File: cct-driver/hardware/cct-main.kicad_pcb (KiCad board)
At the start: 2 copper layers, 130 x 164 mm, 217 parts, among them J1 C707824, J10 C37815, J11 C474923, J2 C165948, J3 C441333, J4 C441333, J5 C441333, J6 C441333, J7 C441333, J8 C441333, J9 C2906270, Q1 C3281500, Q10 C2890395, Q11 C2890395, Q12 C2890395, Q13 C2890395, Q14 C2890395, Q15 C2890395, Q16 C2890395, Q17 C2890395, Q18 C2890395, Q2 C3281500, Q3 C20526, Q4 C2146, Q5 C2146, Q6 C20526, Q7 C2890395, Q8 C2890395, Q9 C2890395, SW1 C318884, SW2 C318884, U1 C2864837, U2 C524806, U3 C6186, U4 C701341, U5 C84681, U6 C52140501, U7 C52140501

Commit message: v2 布线:逻辑区的近距离连线铺了一批,未连接 133 → 114,短路仍然是 0
新增一个 `wire()` 小工具:按顺序把同一个网络的几只脚串起来,支持 L 形与 Z 形拐角。
用它铺完了「两脚就在隔壁」的那批线:干接点四路(端子 → 串阻 → 上拉 + 消抖)、
I2C 上拉、Type-C 的 CC 下拉、状态灯、buck 的 FB 分压。

**踩到并记下来的一条**:这些两端元件的**另一只脚常常正好落在 L 形的拐角上** ——
所以很多地方非 Z 形不可,而有些连 Z 形都绕不开(A3/A4 那两块小件排得密,
行距 3.0mm、脚距 1.5mm)。凡是绕不开的,我**没有硬塞**,而是在脚本里标成
`# TODO(下一轮)` 并写清原因,一条条留着:USB 差分对、自动下载那四条、
COMP/COMP_Z、EN 分压、V5_BUCK/V5_SYS 那一串、V24_LOGIC 到 VIN 陶瓷、V3P3 那一串。
下一轮要么给它们单独规划走线,要么把那两块的行距拉开 —— 这是设计决定,不是试出来的。

    走线 488 段 · 过孔 182 颗 · 覆铜 16 块
    短路 0 · 走线交叉 0
    未连接 114 条(12 路 PWM 还整体没布,那要单独规划车道)
    网表与原理图仍然 524 条零差异

Co-Authored-By: Claude <noreply@anthropic.com>
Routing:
- net I2C_SDA: track 0.00 -> 12.6 mm
- net SW_T4: track 0.00 -> 11.2 mm
- net SW_T3: track 0.00 -> 9.25 mm
- net I2C_SCL: track 0.00 -> 9.05 mm
- net SW_T1: track 0.00 -> 8.67 mm
- net CC1: track 0.00 -> 8.53 mm
- net LED1_K: track 0.00 -> 8.50 mm
- net SW_IN4: track 0.00 -> 8.45 mm
- net SW_IN3: track 0.00 -> 8.45 mm
- net SW_IN2: track 0.00 -> 8.45 mm
- net SW_IN1: track 0.00 -> 8.45 mm
- net SW_NODE: track 0.00 -> 8.42 mm
- net SW_T2: track 0.00 -> 7.29 mm
- net FB_5V: track 0.00 -> 4.50 mm
- net CC2: track 0.00 -> 3.53 mm

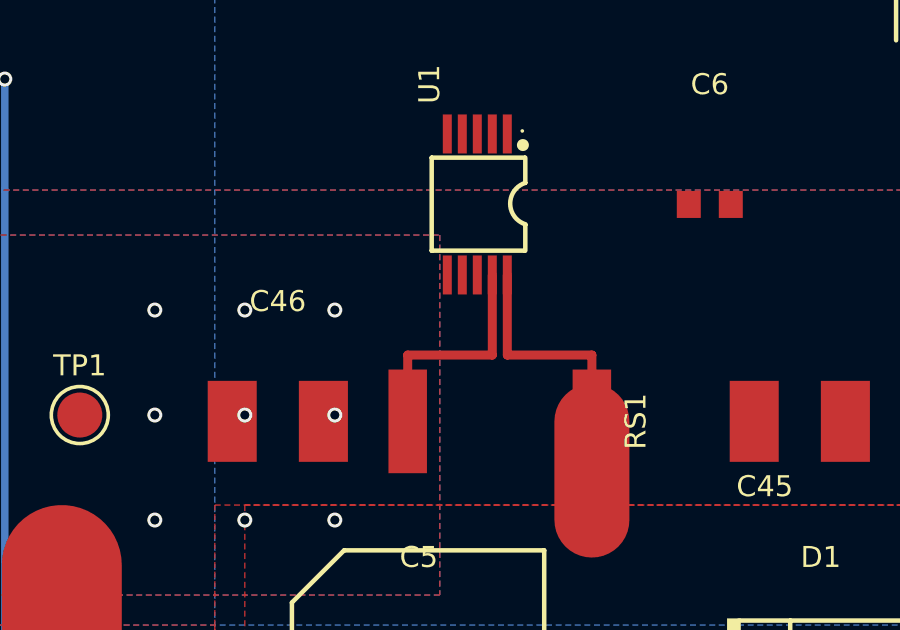
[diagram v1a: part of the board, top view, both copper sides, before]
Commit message: 跟上原理图与封装那两处修正:F1 的映射覆盖撤掉、U1 VBUS 进网表
昨晚报的两件事都有人改了(57dace4 / 8423f9e),这一版把板子这边跟上:

- **F1 的 PAD_GROUPS 覆盖撤掉了。** 库封装已经改成「左夹两盘都编号 1、右夹两盘
  都编号 2」—— 这本来就是 KiCad 表达「一个端子多个焊盘」的正式写法,比在生成器里
  写一张覆盖表干净。**留着那张表反而危险**:它会把编号 2 当成「左夹的第二根脚」,
  在新封装上正好把进线喂到右夹去,等于换个方向再短一次。
- **U1 的 VBUS 接上之后网表从 524 条变 525 条**,板上 U1 的 8 脚不再悬空。
  `verify_netlist_v2.py` 重新跑:**零差异**。
- `check-multipad-mapping.py` 里那条「当前板复核」改成**按几何判、不按编号判**:
  编号会随封装修版变(老的 1/2/3/4、新的 1/1/2/2),但「进线与出线必须落在
  两个不同的夹子上」这条不变。现在它量的是两簇焊盘的 x 中心距(实测 13.48mm)。
  顺带修了 `verify_netlist_v2.py` 里读 PAD_GROUPS 的正则 —— 表空了它会解析炸。

整条流水线重跑:摆位自检全过、位号 0 歧义 0 隐藏、短路 0、未连接 115。

Co-Authored-By: Claude <noreply@anthropic.com>
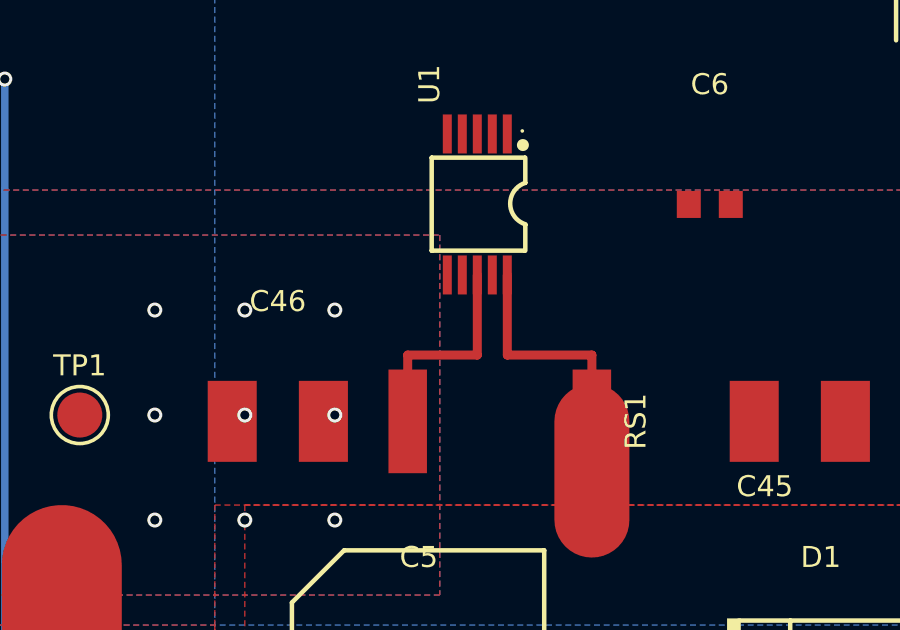
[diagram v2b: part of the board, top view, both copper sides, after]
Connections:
- F1 pad 2: V24_IN -> V24_FUSED
- U1 pad 8: (no net) -> V24_BUS
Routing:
- net V24_BUS: track 41.7 -> 41.2 mm

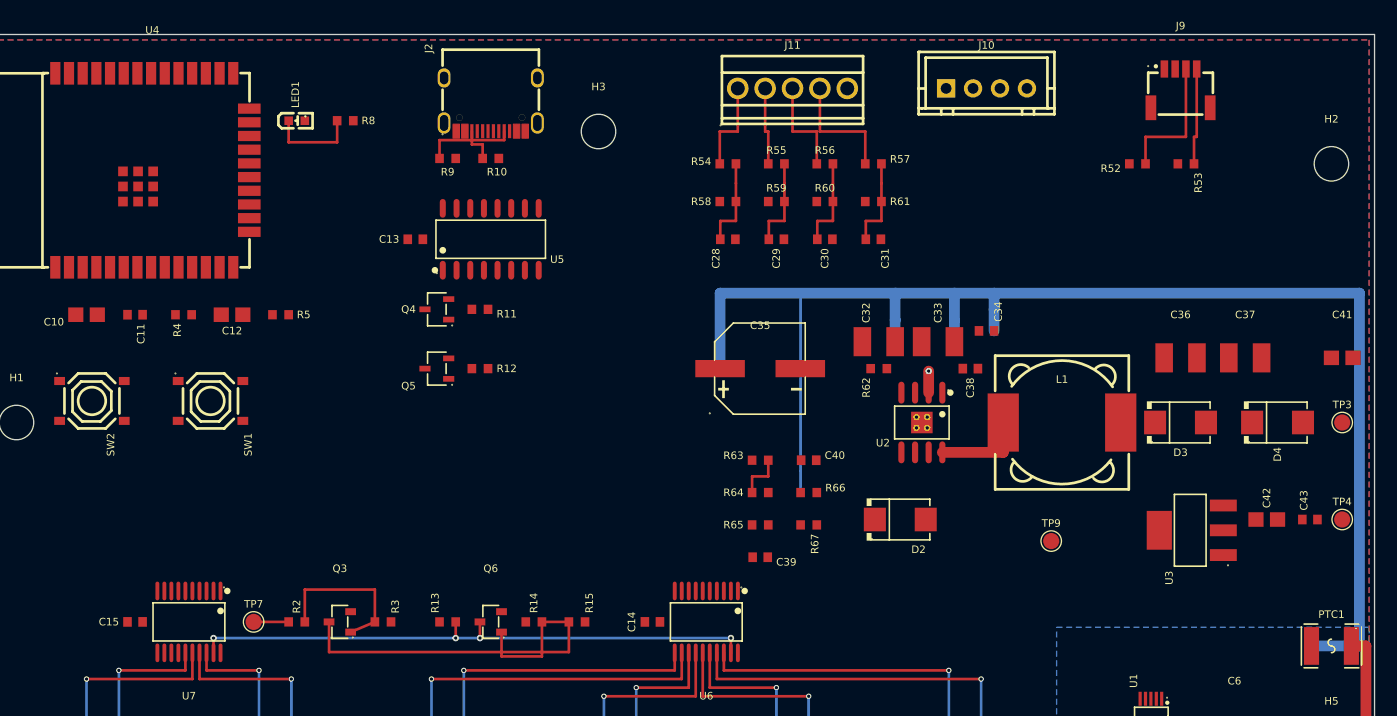
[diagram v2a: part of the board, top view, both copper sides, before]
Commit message: v2 布线:12 路 PWM 成束规划 + 一个会避障的小路由;未连接 115 → 64
两件事。

**一、写了一个会避障的小路由,专门对付逻辑区那些短连线。**
逻辑区的两端元件,**另一只脚常常正好落在 L 形的拐角上**,一条条挑拐点又慢又漏。
现在把「候选拐法 → 逐段查间距 → 第一个干净的就用」写成代码:
候选是**有限且按固定顺序**枚举的(先横后竖 / 先竖后横 / 两族 Z 形 / 一族五点绕行,
外加从焊盘先垂直逃出它那一排的若干出口),所以结果可复现,不是随机试出来的。
它还看得见天线净空和板边留白。**布不通就明说布不通**(记进 UNROUTED,末尾逐条列出),
绝不硬塞 —— 这一版还剩 29 条没布通,全列在脚本输出里。
为了跑得动加了粗网格索引(6mm 一格),整条流水线 5 秒跑完。

**二、12 路 PWM 是一束,必须一起规划,一根根找缝一定互相堵死(试过,只布通 3 根)。**
结构是「底层竖下来 → 顶层横向车道 → 顶层竖下去插进驱动器输入脚」,
车道的 y **按目标 x 从右到左依次下移** —— 这样每根线最后那一竖只会经过比自己
更靠右的车道所在的 x,而那些车道早就在它上方拐走了,一根都不交叉。
源头那一竖放底层,与顶层车道天然不打架;U4 上下两排会撞 x,所以先分互不重叠的竖道。

    走线 738 段 · 过孔 218 颗 · 覆铜 16 块
    **短路 0 · 走线交叉 0**
    未连接 64 条(上一版 115)
    DRC 合计 172 条

Co-Authored-By: Claude <noreply@anthropic.com>
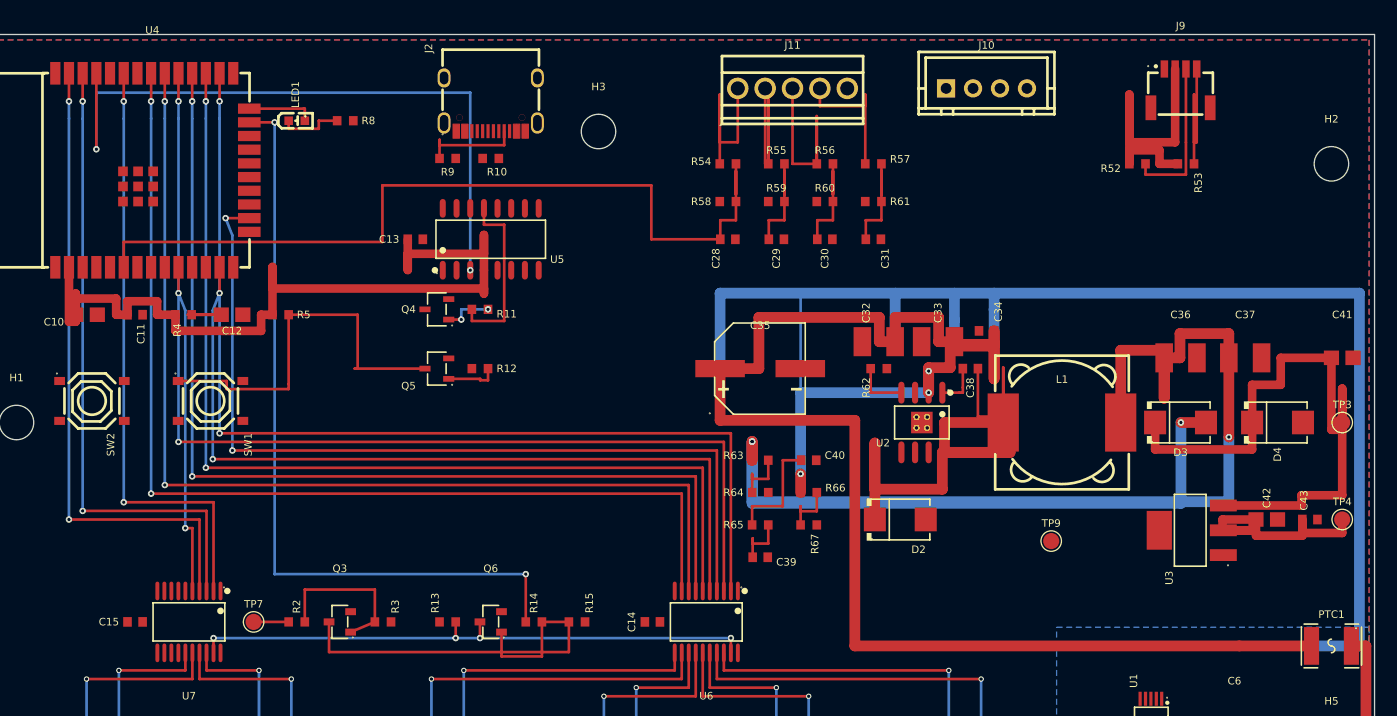
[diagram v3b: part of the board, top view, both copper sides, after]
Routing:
- net V24_LOGIC: track 136.5 -> 294.5 mm, vias 1 -> 3
- net V5_BUCK: track 0.00 -> 151.4 mm, vias 0 -> 4
- net V3P3: track 0.00 -> 133.9 mm
- net CH1_WW: track 0.00 -> 98.6 mm, vias 0 -> 2
- net CH4_WW: track 0.00 -> 97.3 mm, vias 0 -> 2
- net CH4_CW: track 0.00 -> 96.6 mm, vias 0 -> 2
- net CH1_CW: track 0.00 -> 95.5 mm, vias 0 -> 2
- net CH3_WW: track 0.00 -> 94.7 mm, vias 0 -> 2
- net CH3_CW: track 0.00 -> 94.1 mm, vias 0 -> 2
- net CH2_CW: track 0.00 -> 81.9 mm, vias 0 -> 2
- net CH2_WW: track 0.00 -> 76.3 mm, vias 0 -> 2
- net SW_IN1: track 8.45 -> 80.7 mm
- net OE_CTRL: track 0.00 -> 72.0 mm, vias 0 -> 2
- net U0TXD: track 0.00 -> 63.5 mm, vias 0 -> 2
- net V5_SYS: track 0.00 -> 60.7 mm
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
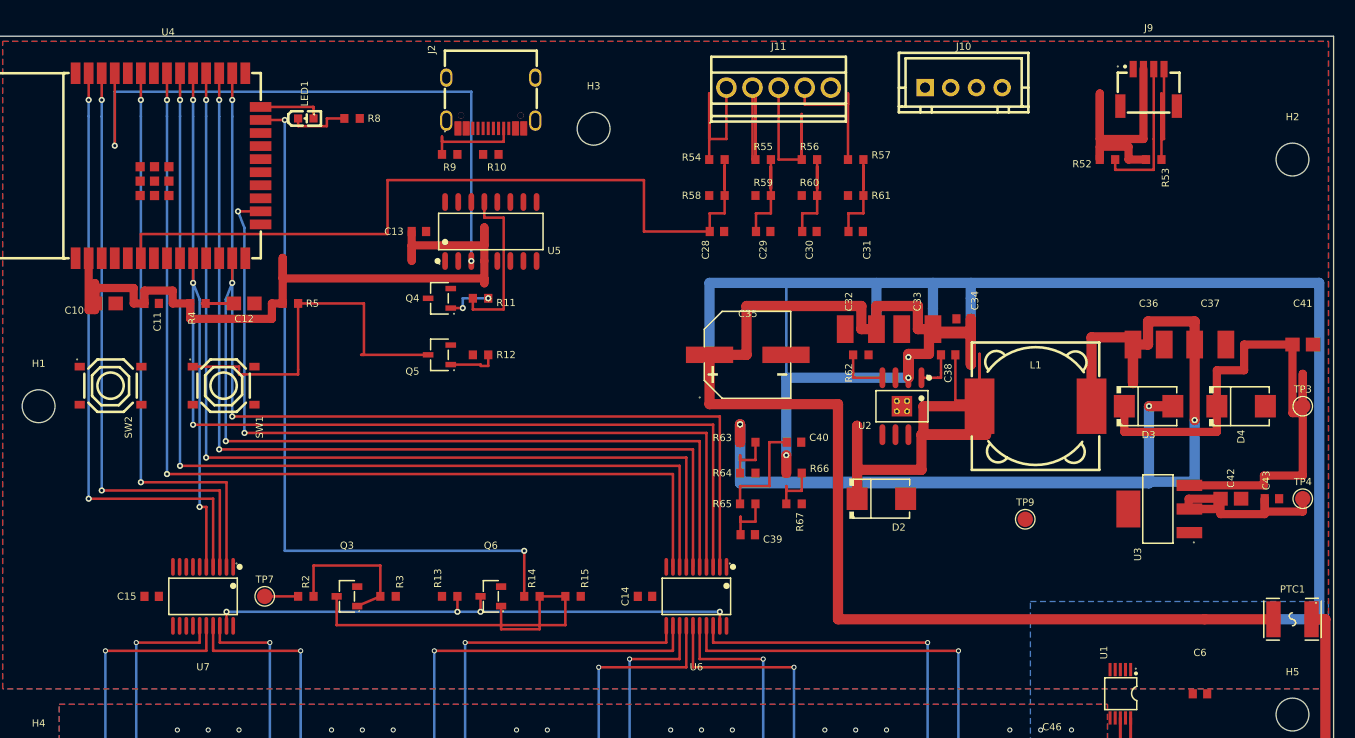
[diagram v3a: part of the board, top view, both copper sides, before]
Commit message: v2 布线:接口那 8 根横穿全板的信号也成束规划;未连接 64 → 55,短路仍是 0
「MCU 在左上、对外接口在右上」这个楼层规划有个必然代价:干接点四路 + I2C 两路 +
UART2 两路,共 **8 根要从 x≈70–112 横穿回 U4 下排 x≈11–22**。跟 PWM 那束一样成束规划:
源头顶层出脚 → 底层竖下来 → **顶层横向车道(每根一条自己的 y)** → 竖上去插进 U4。
车道 y 按目标 x 从右到左依次下移,于是一根都不交叉。

为了腾出 y 23.2–27.8 这条带,动了三处摆位(都在自检里复核过):
- A1 那排小件下移 3.5mm、C35 下移 1.5mm
- **自动下载那四件(Q4/Q5/R11/R12)下移到 y46.5/49.8** —— 它们原来正好坐在
  PWM 的横向车道带(y37–46)上
- buck 的 VIN 陶瓷整排下移到 y30.5 —— 原来坐在接口总线带上;
  D2 跟着上移 2mm 把开关环路收回 1.78cm²(<2cm² 的硬要求)

另外三处走线冲突逐个查清了根因,不是挪一挪试出来的:
- **U4 上下两排会出现同一个 x** —— 下排那两根 PWM 的换层孔只能停在 y22.55,
  再往下就撞上接口总线带了
- **沿右板边下行的两条 I2C,外面那条要拐得更靠下**,否则它的竖直段横穿里面那条的横道
- **V24_LOGIC 不能横穿右板边那两条 I2C 竖道**,改成先在 y57.5 横过来再上到体电容

    走线 772 段 · 过孔 250 颗 · 覆铜 16 块
    **短路 0 · 走线交叉 0**
    未连接 55 条;小路由还有 17 条没布通(逐条列在脚本输出里)
    网表与原理图 525 条零差异

Co-Authored-By: Claude <noreply@anthropic.com>
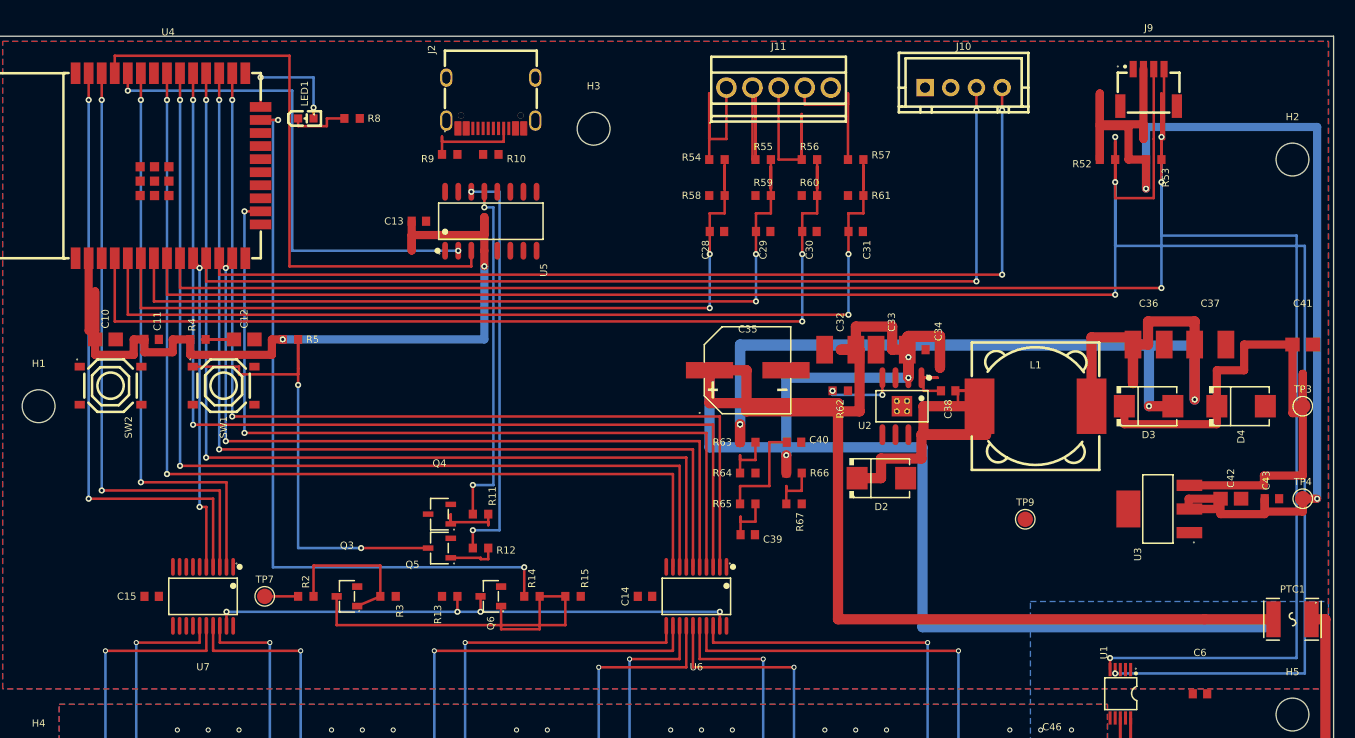
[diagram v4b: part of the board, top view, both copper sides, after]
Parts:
- moved Q4 21.0 mm to (43.0, 46.5)
- moved R11 21.0 mm to (47.0, 46.5)
- moved Q5 18.8 mm to (43.0, 49.8)
- moved R12 18.8 mm to (47.0, 49.8)
- moved C34 4.24 mm to (91.0, 30.5)
- moved R62 4.03 mm to (82.0, 34.5)
- moved C10 3.50 mm to (10.5, 29.5)
- moved C11 3.50 mm to (15.0, 29.5)
- moved C12 3.50 mm to (24.0, 29.5)
- moved C38 3.50 mm to (92.5, 34.5)
- moved R4 3.50 mm to (19.5, 29.5)
- moved R5 3.50 mm to (28.5, 29.5)
- moved C33 3.20 mm to (87.0, 30.5)
- moved C32 2.83 mm to (82.0, 30.5)
- moved D2 2.00 mm to (86.0, 43.0)
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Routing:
- net I2C_SDA: track 14.6 -> 224.1 mm, vias 0 -> 4
- net I2C_SCL: track 17.9 -> 214.1 mm, vias 0 -> 4
- net UART2_TX: track 0.00 -> 96.0 mm, vias 0 -> 2
- net UART2_RX: track 0.00 -> 96.0 mm, vias 0 -> 2
- net SW_IN4: track 12.8 -> 96.5 mm, vias 0 -> 2
- net SW_IN3: track 12.8 -> 94.6 mm, vias 0 -> 2
- net V3P3: track 133.9 -> 206.4 mm, vias 0 -> 4
- net SW_IN2: track 12.8 -> 82.4 mm, vias 0 -> 2
- net V24_LOGIC: track 294.5 -> 237.9 mm
- net U0RXD: track 0.00 -> 49.4 mm, vias 0 -> 2
- net RTS: track 0.00 -> 40.0 mm, vias 0 -> 2
- net SW_NODE: track 58.1 -> 40.0 mm
- net DTR: track 16.4 -> 34.2 mm, vias 0 -> 2
- net IO0: track 36.1 -> 47.3 mm, vias 0 -> 2
- net LED_STATUS: track 6.27 -> 12.0 mm, vias 0 -> 2
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
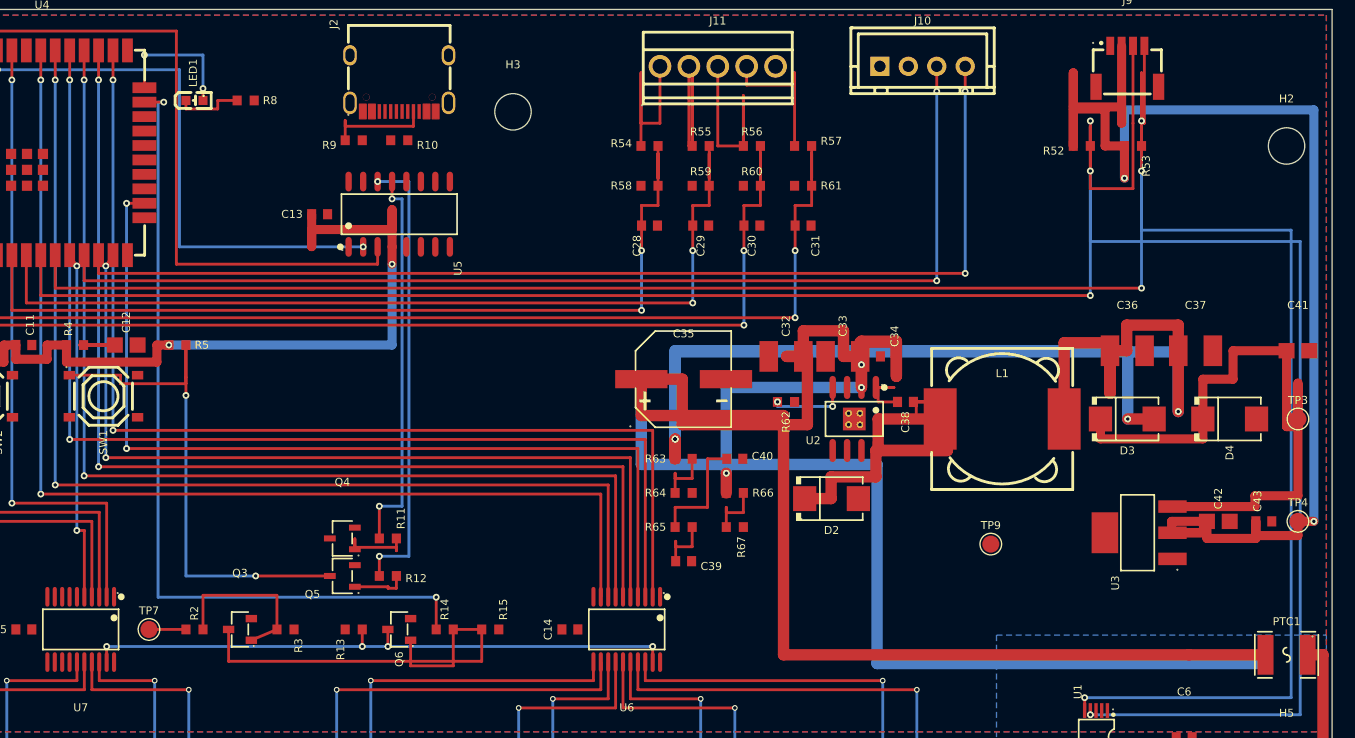
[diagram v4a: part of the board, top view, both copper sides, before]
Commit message: v2 布线:跨区干线改成「先查干净再落笔」;未连接 55 → 47,短路仍是 0
这一版把手写的跨区干线也纳入同一套纪律:新增 `corridor()` —— 从两端各竖出一小截换到
底层、横过去、再竖回去,**走廊位置和逃逸点都是按固定顺序枚举、逐个查过间距才落笔的**;
一条都不干净就记进 DIRTY,末尾逐条报出来,和 `auto()` 一样绝不硬塞。

**踩到并记下来的一条:干线必须排在小连线前面挑路。** 先让 `auto()` 把附近的短线布完,
再回头布这些两头被密集焊盘夹住、中间要横穿半块板的干线,那一两条能走的走廊早被占了 ——
FB_5V 和 COMP 就是这么栽的(实测:调换顺序之后两条都通了)。

顺带按实测数据挪了几处摆位,都是「差 0.2mm」级的:
buck 的 VIN 陶瓷整排上移 0.5mm(EN 分压的换层孔离它只差 0.01mm)、
自动下载那四件排成一行压在 PWM 车道带以下、V5_SYS 横轨改走底层(顶层被 12 根 PWM 穿过去)。

    走线 790 段 · 过孔 260 颗 · 覆铜 16 块
    **短路 0 · 走线交叉 0**
    未连接 47 条;明确报出布不通的 11 条(6 条小连线 + 5 条干线)
    网表与原理图 525 条零差异

Co-Authored-By: Claude <noreply@anthropic.com>
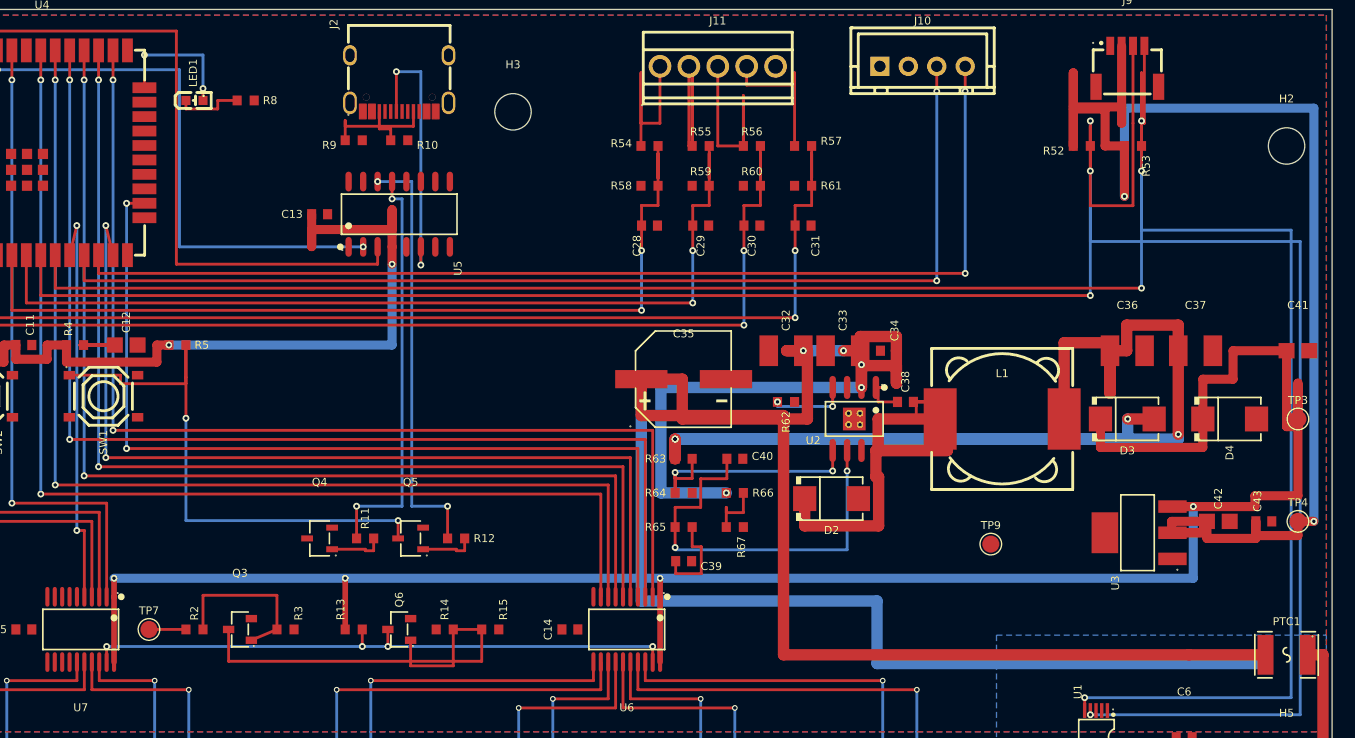
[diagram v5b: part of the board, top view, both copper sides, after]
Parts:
- moved Q5 6.85 mm to (49.0, 46.5)
- moved R12 6.85 mm to (53.0, 46.5)
- moved Q4 2.00 mm to (41.0, 46.5)
- moved R11 2.00 mm to (45.0, 46.5)
- moved C32 0.50 mm to (82.0, 30.0)
- moved C33 0.50 mm to (87.0, 30.0)
- moved C34 0.50 mm to (91.0, 30.0)
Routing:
- net V5_SYS: track 59.2 -> 263.6 mm, vias 0 -> 4
- net V24_LOGIC: track 237.9 -> 164.2 mm, vias 3 -> 5
- net OE_CTRL: track 73.0 -> 0.00 mm, vias 2 -> 0
- net COMP: track 10.5 -> 36.4 mm, vias 0 -> 2
- net USB_DM: track 0.00 -> 24.2 mm, vias 0 -> 2
- net V5_BUCK: track 151.3 -> 128.8 mm
- net FB_5V: track 5.43 -> 23.0 mm, vias 0 -> 2
- net SW_NODE: track 40.0 -> 45.3 mm
- net CH2_WW: track 76.3 -> 81.4 mm
- net CH6_WW: track 30.9 -> 36.0 mm
- net CC2: track 0.00 -> 3.53 mm
- net V3P3: track 206.4 -> 209.9 mm
- net I2C_SDA: track 224.1 -> 227.1 mm
- net COMP_Z: track 5.41 -> 8.25 mm
- net IO0: track 47.3 -> 50.0 mm
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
